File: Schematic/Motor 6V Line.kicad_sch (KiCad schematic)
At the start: 30 parts, among them Q15 CSD19531Q5AT, Q16 CSD19531Q5AT, U24 TPS40305DRCT

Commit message: Added DigiKey to BOM
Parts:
- C109: DigiKey Link (none) -> https://www.digikey.com/short/2nhzzz3n; DigiKey Part Number (none) -> CL10B104MB8NNNC; DigiKey Price per Unit (none) -> 0.08; Link https://mou.sr/3JWJm45 -> (none); Manufactaurer Part Number (none) -> CL10B104MB8NNNC; Manufacturer Part Number CL10B104MB8NNNC -> (none); Mouser Link (none) -> https://mou.sr/3JWJm45; Mouser Part Number (none) -> 187-CL10B104MB8NNNC; Mouser Price per Unit (none) -> 0.10; Price per Unit 0.10 -> (none); Supplier Mouser -> (none); Supplier Part Number 187-CL10B104MB8NNNC -> (none)
- L3: Manufacturer_Part_Number SLC1480-441MLD -> (none); Mouser Part Number 994-SLC1480-441MLD -> (none)
- Q15, Q16: Manufacturer_Part_Number CSD19531Q5AT -> (none); Mouser Part Number 595-CSD19531Q5AT -> (none)
- R86: DigiKey Link (none) -> https://www.digikey.com/short/wc78wrb5; DigiKey Part Number (none) -> 13-AC0603FR-7W4K7LTR-ND; DigiKey Price per Unit (none) -> 0.10; Link https://mou.sr/4n9UsBp -> (none); Manufactaurer Part Number (none) -> AC0603FR-7W4K7L; Manufacturer Part Number AC0603FR-7W4K7L -> (none); Mouser Link (none) -> https://mou.sr/4n9UsBp; Mouser Part Number (none) -> 603-AC0603FR-7W4K7L; Mouser Price per Unit (none) -> 0.10; Price per Unit 0.10 -> (none); Supplier Mouser -> (none); Supplier Part Number 603-AC0603FR-7W4K7L -> (none)
- R87: DigiKey Link (none) -> https://www.digikey.com/short/9894ptm2; DigiKey Part Number (none) -> YAG4804TR-ND; DigiKey Price per Unit (none) -> 0.10; Link https://mou.sr/3IjcfqA -> (none); Manufactaurer Part Number (none) -> RT0603DRE071K37L; Manufacturer Part Number RT0603DRE071K37L -> (none); Mouser Link (none) -> https://mou.sr/3IjcfqA; Mouser Part Number (none) -> 603-RT0603DRE071K37L; Mouser Price per Unit (none) -> 0.10; Price per Unit 0.10 -> (none); Supplier Mouser -> (none); Supplier Part Number 603-RT0603DRE071K37L -> (none)
- R88: DigiKey Link (none) -> https://www.digikey.com/short/z53721ph; DigiKey Part Number (none) -> 13-RT0603FRE077K68LTR-ND; DigiKey Price per Unit (none) -> 0.10; Link https://mou.sr/4pmZ9Jx -> (none); Manufactaurer Part Number (none) -> RT0603FRE077K68L; Manufacturer Part Number RT0603FRE077K68L -> (none); Mouser Link (none) -> https://mou.sr/4pmZ9Jx; Mouser Part Number (none) -> 603-RT0603FRE077K68L; Mouser Price per Unit (none) -> 0.10; Price per Unit 0.10 -> (none); Supplier Mouser -> (none); Supplier Part Number 603-RT0603FRE077K68L -> (none)
- R89: DigiKey Link (none) -> https://www.digikey.com/short/3dpf4t73; DigiKey Part Number (none) -> P309DBTR-ND; DigiKey Price per Unit (none) -> 0.10; Link https://mou.sr/4mbJQRa -> (none); Manufactaurer Part Number (none) -> ERA-3AEB3090V; Manufacturer Part Number ERA-3AEB3090V -> (none); Mouser Link (none) -> https://mou.sr/4mbJQRa; Mouser Part Number (none) -> 667-ERA-3AEB3090V; Mouser Price per Unit (none) -> 0.10; Price per Unit 0.10 -> (none); Supplier Mouser -> (none); Supplier Part Number 667-ERA-3AEB3090V -> (none)
- R90: DigiKey Link (none) -> N/A; DigiKey Part Number (none) -> N/A; DigiKey Price per Unit (none) -> N/A; Link https://mou.sr/463dpQf -> (none); Manufactaurer Part Number (none) -> RCA060310K0FKEC; Manufacturer Part Number RCA060310K0FKEC -> (none); Mouser Link (none) -> https://mou.sr/463dpQf; Mouser Part Number (none) -> 71-RCA060310K0FKEC; Mouser Price per Unit (none) -> 0.10; Price per Unit 0.10 -> (none); Supplier Mouser -> (none); Supplier Part Number 71-RCA060310K0FKEC -> (none)
- R91: DigiKey Link (none) -> https://www.digikey.com/short/tbq0chd9; DigiKey Part Number (none) -> MCT0603-1.0K-MDTR-ND; DigiKey Price per Unit (none) -> 0.10; Link https://mou.sr/4pjaV7O -> (none); Manufactaurer Part Number (none) -> MCT0603MD1001DP500; Manufacturer Part Number MCT0603MD1001DP500 -> (none); Mouser Link (none) -> https://mou.sr/4pjaV7O; Mouser Part Number (none) -> 594-MCT0603MD1001DP5; Mouser Price per Unit (none) -> 0.10; Price per Unit 0.10 -> (none); Supplier Mouser -> (none); Supplier Part Number 594-MCT0603MD1001DP5 -> (none)
- U24: footprint TPS40305DRCT -> TPS40305DRCT:TPS40305DRCT; DigiKey Link (none) -> https://www.digikey.com/short/zd2zm3zm; DigiKey Part Number (none) -> 296-25487-2-ND; DigiKey Price per Unit (none) -> 2.68; Manufactaurer Part Number (none) -> TPS40305DRCT; Manufacturer_Part_Number TPS40305DRCT -> (none); Mouser Link (none) -> https://mou.sr/4dYeVVm; Mouser Price per Unit (none) -> 2.68

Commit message: need to do Qs now
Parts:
- removed L3: SLC1480-441MLD, SLC1480441MLD, symbol SLC1480-441MLD:SLC1480-441MLD
- added L3: SPB1308-R44M, SPB1308-R44M:INDM135130X800N, symbol Device:L
- C109: DigiKey Part Number CL10B104MB8NNNC -> (none)
- Q15, Q16: footprint CSD19531Q5AT -> CSD19531Q5AT:CSD19531Q5AT; DigiKey Link (none) -> https://www.digikey.com/short/jj3c34th; DigiKey Price per Unit (none) -> 3.15; Manufactaurer Part Number (none) -> CSD19531Q5AT; Mouser Link (none) -> https://mou.sr/4mgdEMD; Mouser Part Number (none) -> 595-CSD19531Q5AT; Mouser Price per Unit (none) -> 3.21
- R86: DigiKey Part Number 13-AC0603FR-7W4K7LTR-ND -> (none)
- R87: DigiKey Part Number YAG4804TR-ND -> (none)
- R88: DigiKey Part Number 13-RT0603FRE077K68LTR-ND -> (none)
- R89: DigiKey Part Number P309DBTR-ND -> (none)
- R91: DigiKey Part Number MCT0603-1.0K-MDTR-ND -> (none)
- U22: renamed from U24; DigiKey Part Number 296-25487-2-ND -> (none)
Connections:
- net P6V0: now also L3.2
- net at C109.2, Q15.1 (S), Q15.2 (S)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: now also L3.1
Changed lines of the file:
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@@
 			)
 		)
-		(property "DigiKey Part Number" "13-AC0603FR-7W4K7LTR-ND"
+		(property "DigiKey Part Number" ""
 			(at 71.12 109.22 0)
 			(effects
@@
 			)
 		)
-		(property "Footprint" "CSD19531Q5AT"
+		(property "Footprint" "CSD19531Q5AT:CSD19531Q5AT"
 			(at 193.04 207.95 0)
 			(effects
@@
 			)
 		)
-		(property "Mouser Part Number" ""
+		(property "Mouser Part Number" "595-CSD19531Q5AT"
 			(at 193.04 607.95 0)
 			(effects
@@
 			)
 		)
-		(property "DigiKey Link" ""
+		(property "DigiKey Link" "https://www.digikey.com/short/jj3c34th"
 			(at 171.45 113.03 0)
 			(effects
@@
 			)
 		)
+		(property "DigiKey Price per Unit" "3.15"
+			(at 171.45 113.03 0)
+			(effects
+				(font
+					(size 1.27 1.27)
+				)
+				(hide yes)
+			)
+		)
+		(property "Manufactaurer Part Number" "CSD19531Q5AT"
+			(at 171.45 113.03 0)
+			(effects
+				(font
+					(size 1.27 1.27)
+				)
+				(hide yes)
+			)
+		)
+		(property "Mouser Link" "https://mou.sr/4mgdEMD"
+			(at 171.45 113.03 0)
+			(effects
+				(font
+					(size 1.27 1.27)
+				)
+				(hide yes)
+			)
+		)
+		(property "Mouser Price per Unit" "3.21"
+			(at 171.45 113.03 0)
+			(effects
+				(font
+					(size 1.27 1.27)
+				)
+				(hide yes)
+			)
+		)
 		(pin "2"
 		)
@@
 	)
 	(symbol
-		(lib_id "SLC1480-441MLD:SLC1480-441MLD")
-		(at 204.47 101.6 0)
-		(unit 1)
-		(exclude_from_sim no)
-		(in_bom yes)
-		(on_board yes)
-		(dnp no)
-		(property "Reference" "L3"
-			(at 199.39 100.076 0)
-			(effects
-				(font
-					(size 1.27 1.27)
-				)
-				(justify left top)
-			)
-		)
-		(property "Value" "SLC1480-441MLD"
-			(at 207.01 99.822 0)
-			(effects
-				(font
-					(size 1.27 1.27)
-				)
-				(justify left top)
-			)
-		)
-		(property "Footprint" "SLC1480441MLD"
-			(at 220.98 197.79 0)
-			(effects
-				(font
-					(size 1.27 1.27)
-				)
-				(justify left top)
-				(hide yes)
-			)
-		)
-		(property "Datasheet" "https://www.mouser.cn/datasheet/2/597/slc1480-270715.pdf"
-			(at 220.98 297.79 0)
-			(effects
-				(font
-					(size 1.27 1.27)
-				)
-				(justify left top)
-				(hide yes)
-			)
-		)
-		(property "Description" "Power Inductors - SMD 440nH Shld 20% 55A 210mOhms"
-			(at 204.47 101.6 0)
-			(effects
-				(font
-					(size 1.27 1.27)
-				)
-				(hide yes)
-			)
-		)
-		(property "Height" "8"
-			(at 220.98 497.79 0)
-			(effects
-				(font
-					(size 1.27 1.27)
-				)
-				(justify left top)
-				(hide yes)
-			)
-		)
-		(property "Mouser Part Number" ""
-			(at 220.98 597.79 0)
-			(effects
-				(font
-					(size 1.27 1.27)
-				)
-				(justify left top)
-				(hide yes)
-			)
-		)
-		(property "Mouser Price/Stock" "https://www.mouser.co.uk/ProductDetail/Coilcraft/SLC1480-441MLD?qs=zCSbvcPd3pa7ldcZAzcJ6A%3D%3D"
-			(at 220.98 697.79 0)
-			(effects
-				(font
-					(size 1.27 1.27)
-				)
-				(justify left top)
-				(hide yes)
-			)
-		)
-		(property "Manufacturer_Name" "COILCRAFT"
-			(at 220.98 797.79 0)
-			(effects
-				(font
-					(size 1.27 1.27)
-				)
-				(justify left top)
-				(hide yes)
-			)
-		)
-		(property "DigiKey Link" ""
-			(at 204.47 101.6 0)
-			(effects
-				(font
-					(size 1.27 1.27)
-				)
-				(hide yes)
-			)
-		)
-		(property "DigiKey Part Number" ""
-			(at 204.47 101.6 0)
-			(effects
-				(font
-					(size 1.27 1.27)
-				)
-				(hide yes)
-			)
-		)
-		(pin "1"
-		)
-		(pin "2"
-		)
-		(instances
-			(project ""
-				(path "/fc8533bc-25dd-4c20-9b4c-ffebebd6739b/f73d6367-f3ba-42df-a3ea-bd155f1c219f/59156c40-dbaf-44c5-bcaf-7991575a4ded"
-					(reference "L3")
-					(unit 1)
-				)
-			)
-		)
-	)
-	(symbol
 		(lib_id "Device:C")
 		(at 38.1 105.41 0)
@@
 			)
 		)
-		(property "DigiKey Part Number" "13-RT0603FRE077K68LTR-ND"
+		(property "DigiKey Part Number" ""
 			(at 173.99 118.11 0)
 			(effects
@@
 			)
 		)
-		(property "DigiKey Part Number" "YAG4804TR-ND"
+		(property "DigiKey Part Number" ""
 			(at 91.44 120.65 0)
 			(effects
@@
 	)
 	(symbol
+		(lib_id "Device:L")
+		(at 204.47 101.6 90)
+		(unit 1)
+		(exclude_from_sim no)
+		(in_bom yes)
+		(on_board yes)
+		(dnp no)
+		(property "Reference" "L3"
+			(at 200.406 100.584 90)
+			(effects
+				(font
+					(size 1.27 1.27)
+				)
+			)
+		)
+		(property "Value" "SPB1308-R44M"
+			(at 214.884 100.33 90)
+			(effects
+				(font
+					(size 1.27 1.27)
+				)
+			)
+		)
+		(property "Footprint" "SPB1308-R44M:INDM135130X800N"
+			(at 204.47 101.6 0)
+			(effects
+				(font
+					(size 1.27 1.27)
+				)
+				(hide yes)
+			)
+		)
+		(property "Datasheet" "~"
+			(at 204.47 101.6 0)
+			(effects
+				(font
+					(size 1.27 1.27)
+				)
+				(hide yes)
+			)
+		)
+		(property "Description" "Inductor"
+			(at 204.47 101.6 0)
+			(effects
+				(font
+					(size 1.27 1.27)
+				)
+				(hide yes)
+			)
+		)
+		(property "DigiKey Link" "https://www.digikey.com/short/qjzrmcqw"
+			(at 204.47 101.6 90)
+			(effects
+				(font
+					(size 1.27 1.27)
+				)
+				(hide yes)
+			)
+		)
+		(property "DigiKey Part Number" ""
+			(at 204.47 101.6 90)
+			(effects
+				(font
+					(size 1.27 1.27)
+				)
+				(hide yes)
+			)
+		)
+		(property "DigiKey Price per Unit" "1.58"
+			(at 204.47 101.6 90)
+			(effects
+				(font
+					(size 1.27 1.27)
+				)
+				(hide yes)
+			)
+		)
+		(property "Manufactaurer Part Number" "SPB1308-R44M"
+			(at 204.47 101.6 90)
+			(effects
+				(font
+					(size 1.27 1.27)
+				)
+				(hide yes)
+			)
+		)
+		(property "Mouser Link" "https://mou.sr/3IkWG1C"
+			(at 204.47 101.6 90)
+			(effects
+				(font
+					(size 1.27 1.27)
+				)
+				(hide yes)
+			)
+		)
+		(property "Mouser Part Number" "652-SPB1308-R44M"
+			(at 204.47 101.6 90)
+			(effects
+				(font
+					(size 1.27 1.27)
+				)
+				(hide yes)
+			)
+		)
+		(property "Mouser Price per Unit" "1.89"
+			(at 204.47 101.6 90)
+			(effects
+				(font
+					(size 1.27 1.27)
+				)
+				(hide yes)
+			)
+		)
+		(pin "1"
+		)
+		(pin "2"
+		)
+		(instances
+			(project ""
+				(path "/fc8533bc-25dd-4c20-9b4c-ffebebd6739b/f73d6367-f3ba-42df-a3ea-bd155f1c219f/59156c40-dbaf-44c5-bcaf-7991575a4ded"
+					(reference "L3")
+					(unit 1)
+				)
+			)
+		)
+	)
+	(symbol
 		(lib_id "TPS40305DRCT:TPS40305DRCT")
 		(at 125.73 96.52 0)
@@
 		(on_board yes)
 		(dnp no)
-		(property "Reference" "U24"
+		(property "Reference" "U22"
 			(at 154.686 85.09 0)
 			(effects
@@
 			)
 		)
-		(property "DigiKey Part Number" "296-25487-2-ND"
+		(property "DigiKey Part Number" ""
 			(at 125.73 96.52 0)
 			(effects
@@
 			(project ""
 				(path "/fc8533bc-25dd-4c20-9b4c-ffebebd6739b/f73d6367-f3ba-42df-a3ea-bd155f1c219f/59156c40-dbaf-44c5-bcaf-7991575a4ded"
-					(reference "U24")
+					(reference "U22")
 					(unit 1)
 				)
@@
 			)
 		)
-		(property "Footprint" "CSD19531Q5AT"
+		(property "Footprint" "CSD19531Q5AT:CSD19531Q5AT"
 			(at 193.04 186.36 0)
 			(effects
@@
 			)
 		)
-		(property "Mouser Part Number" ""
+		(property "Mouser Part Number" "595-CSD19531Q5AT"
 			(at 193.04 586.36 0)
 			(effects
@@
 			)
 		)
-		(property "DigiKey Link" ""
+		(property "DigiKey Link" "https://www.digikey.com/short/jj3c34th"
 			(at 171.45 91.44 0)
 			(effects
@@
 			)
 		)
+		(property "DigiKey Price per Unit" "3.15"
+			(at 171.45 91.44 0)
+			(effects
+				(font
+					(size 1.27 1.27)
+				)
+				(hide yes)
+			)
+		)
+		(property "Manufactaurer Part Number" "CSD19531Q5AT"
+			(at 171.45 91.44 0)
+			(effects
+				(font
+					(size 1.27 1.27)
+				)
+				(hide yes)
+			)
+		)
+		(property "Mouser Link" "https://mou.sr/4mgdEMD"
+			(at 171.45 91.44 0)
+			(effects
+				(font
+					(size 1.27 1.27)
+				)
+				(hide yes)
+			)
+		)
+		(property "Mouser Price per Unit" "3.21"
+			(at 171.45 91.44 0)
+			(effects
+				(font
+					(size 1.27 1.27)
+				)
+				(hide yes)
+			)
+		)
 		(pin "2"
 		)
@@
 			)
 		)
-		(property "DigiKey Part Number" "MCT0603-1.0K-MDTR-ND"
+		(property "DigiKey Part Number" ""
 			(at 223.52 116.84 0)
 			(effects
@@
 			)
 		)
-		(property "DigiKey Part Number" "CL10B104MB8NNNC"
+		(property "DigiKey Part Number" ""
 			(at 172.72 99.06 90)
 			(effects
@@
 			)
 		)
-		(property "DigiKey Part Number" "P309DBTR-ND"
+		(property "DigiKey Part Number" ""
 			(at 212.09 106.68 0)
 			(effects

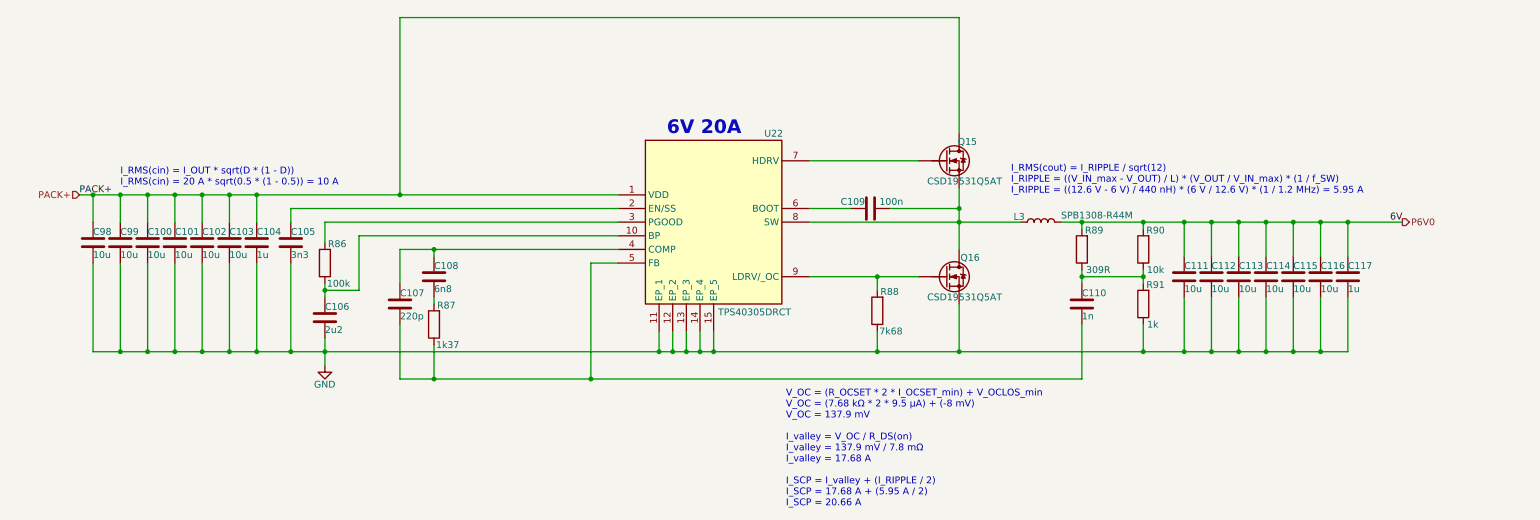
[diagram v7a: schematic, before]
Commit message: Added fuse, more footprints, and cleaned up some things
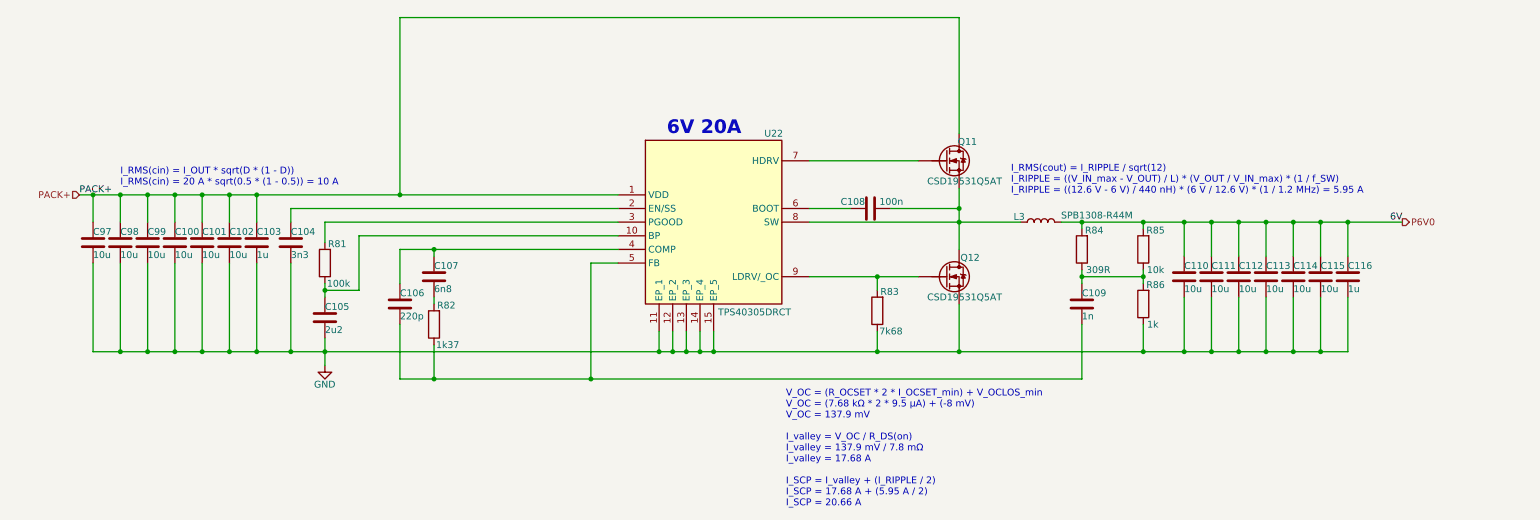
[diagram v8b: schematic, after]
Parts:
- renumbered C101 to C100, C102 to C101, C103 to C102, C104 to C103, C105 to C104, C106 to C105, C107 to C106, C108 to C107, C109 to C108, C110 to C109, C111 to C110, C112 to C111, C113 to C112, C114 to C113, C115 to C114, C116 to C115, C117 to C116, C98 to C97, C99 to C98, C100 to C99, Q15 to Q11, Q16 to Q12, R86 to R81, R87 to R82, R88 to R83, R89 to R84, R90 to R85, R91 to R86
